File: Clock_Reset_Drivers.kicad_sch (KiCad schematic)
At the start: 9 parts, among them J4 2Pin_Header_2.54, U3 SPC5676RDK3MVU1R

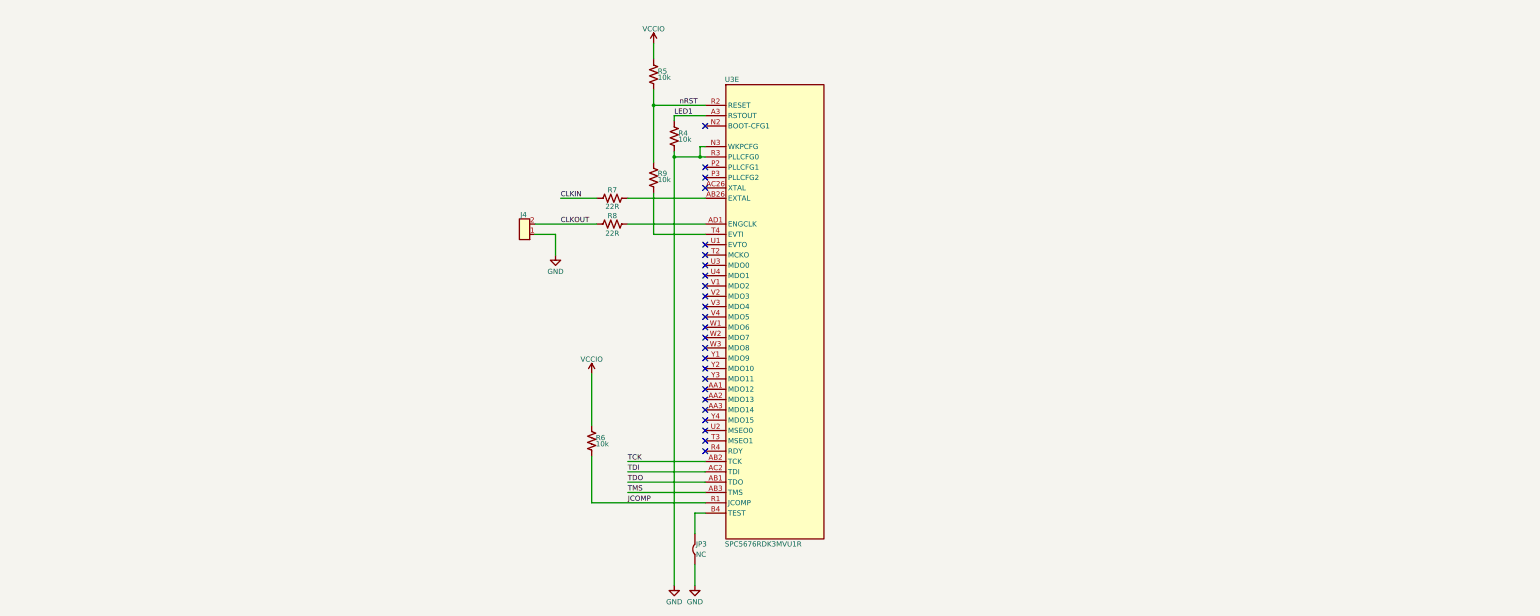
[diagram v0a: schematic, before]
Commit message: draft updated, schematic draft done, pcb issues with size of board and fitting all parts on
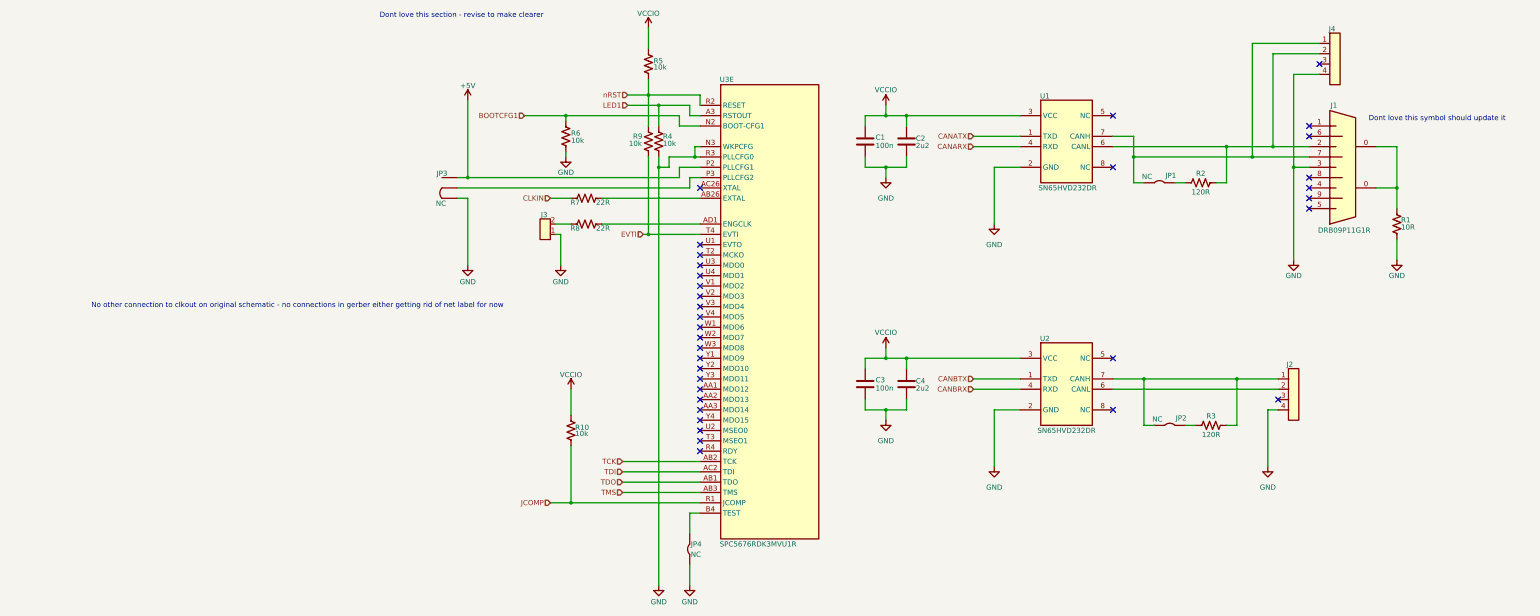
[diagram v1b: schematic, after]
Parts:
- added C1, C3: CAP_100n_16V_0402, Capacitor_SMD:C_0402_1005Metric, symbol nae_caps:CAP_100n_16V_0402
- added C2, C4: CAP_2u2_10V_0603, Capacitor_SMD:C_0603_1608Metric, symbol nae_caps:CAP_2u2_10V_0603
- added J1: DRB09P11G1R, Connector_Dsub:DSUB-9_Male_Horizontal_P2.77x2.84mm_EdgePinOffset9.90mm_Housed_MountingHolesOffset11.32mm, symbol tutorial_2_library:DB9_Connector_male
- added J2, J4: HDR_4_2.54, Connector_PinHeader_1.00mm:PinHeader_1x04_P1.00mm_Vertical, symbol tutorial_2_library:VERT_HDR_4_2.54mm_1
- added JP1, JP2: ~, Jumper:SolderJumper-2_P1.3mm_Bridged2Bar_Pad1.0x1.5mm, symbol tutorial_2_library:Solder_Jumper_2_NC
- added JP3: ~, Jumper:SolderJumper-3_P1.3mm_Bridged2Bar12_Pad1.0x1.5mm, symbol tutorial_2_library:Solder_Jumper_3_NC_1
- added R1: RES_10R_0603, Resistor_SMD:R_0603_1608Metric, symbol 0603_Yageo_Res:RES_10R_0603
- added R2, R3: RES_120R_0603, Resistor_SMD:R_0603_1608Metric, symbol 0603_Yageo_Res:RES_120R_0603
- added R6: RES_10k_0603, Resistor_SMD:R_0603_1608Metric, symbol 0603_Yageo_Res:RES_10k_0603
- added U1, U2: SN65HVD232DR, Package_SO:SOIC-8_3.9x4.9mm_P1.27mm, symbol tutorial_2_library:SN65HVD232DR
- renumbered J4 to J3, JP3 to JP4, R6 to R10
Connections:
- net GND: now also C1.1, C2.1, C3.1, C4.1, J1.3, J2.4, J4.4, JP3.1, R1.1, R6.1, U1.2 (GND), U2.2 (GND)
- net VCCIO: now also C1.2, C2.2, C3.2, C4.2, U1.3 (VCC), U2.3 (VCC)
- net BOOTCFG1: now reaches U3.N2 (BOOT-CFG1)
- net BOOTCFG1: now also R6.2
- net +5V: now reaches U3.P2 (PLLCFG1)
- net +5V: now also JP3.3
- net at U3.P3 (PLLCFG2): now also JP3.2
- net EVTI: now reaches R9.1, U3.T4 (EVTI)
- net CLKOUT: no longer names the net of J3.2, R8.1
- new net: JP1.1, R2.1
- new net: J1.7, J4.1, JP1.2, U1.7 (CANH)
- new net: J1.2, J4.2, R2.2, U1.6 (CANL)
- new net: J1.0, R1.2
- new net: J2.1, JP2.2, R3.2, U2.7 (CANH)
- new net: J2.2, U2.6 (CANL)
- new net: JP2.1, R3.1
- new net CANARX: U1.4 (RXD)
- new net CANATX: U1.1 (TXD)
- new net CANBRX: U2.4 (RXD)
- new net CANBTX: U2.1 (TXD)
- no-connect marks 25 -> 34
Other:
- note added: "Dont love this section - revise to make clearer"
- note added: "Dont love this symbol should update it"
- note added: "No other connection to clkout on original schematic - no connections in gerber either getting rid of net label for now"
- moved on the sheet: J3, JP4, R10, R4, R5, R7, R8, R9, U3E

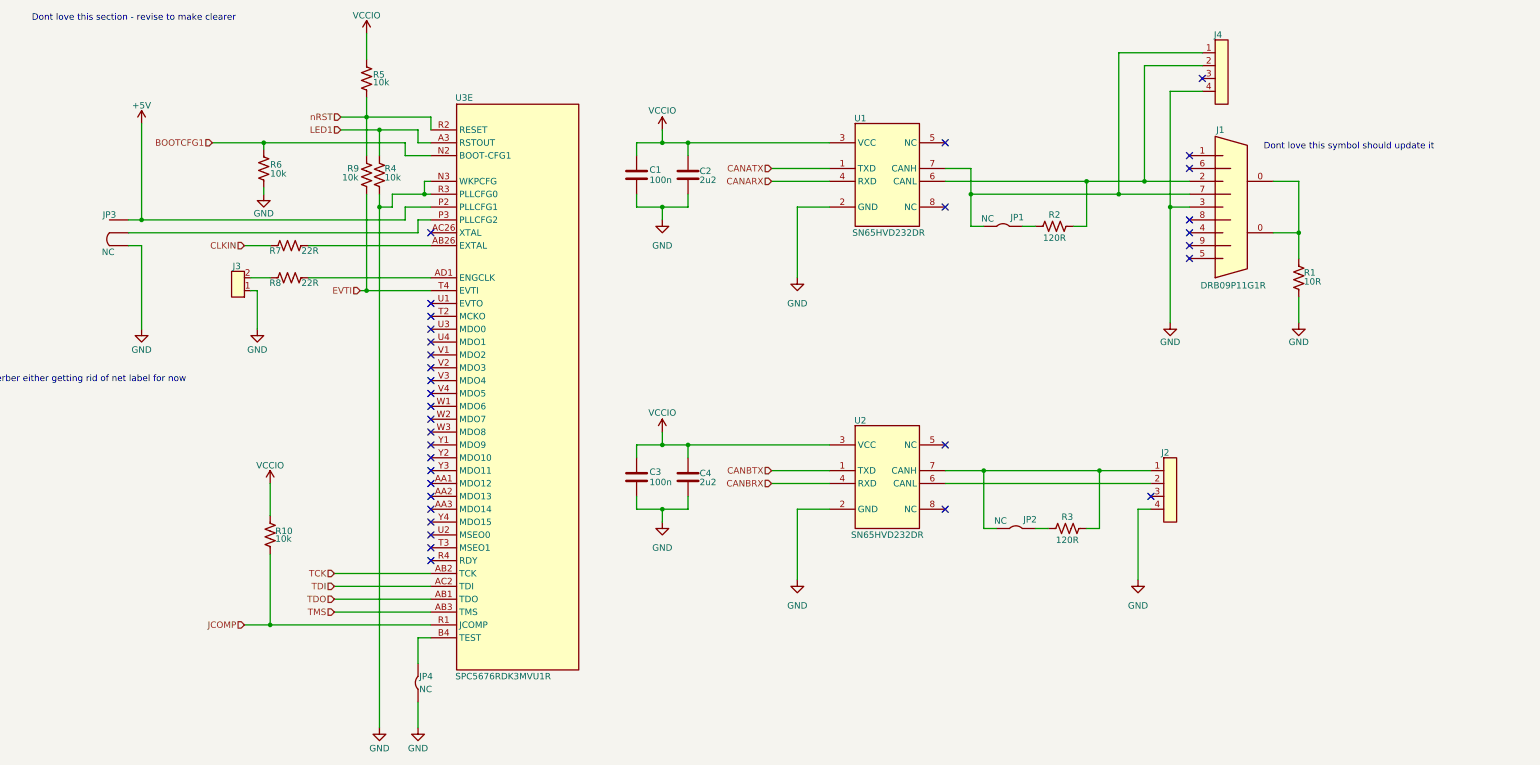
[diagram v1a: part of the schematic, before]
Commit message: updated schematic after library re-organization
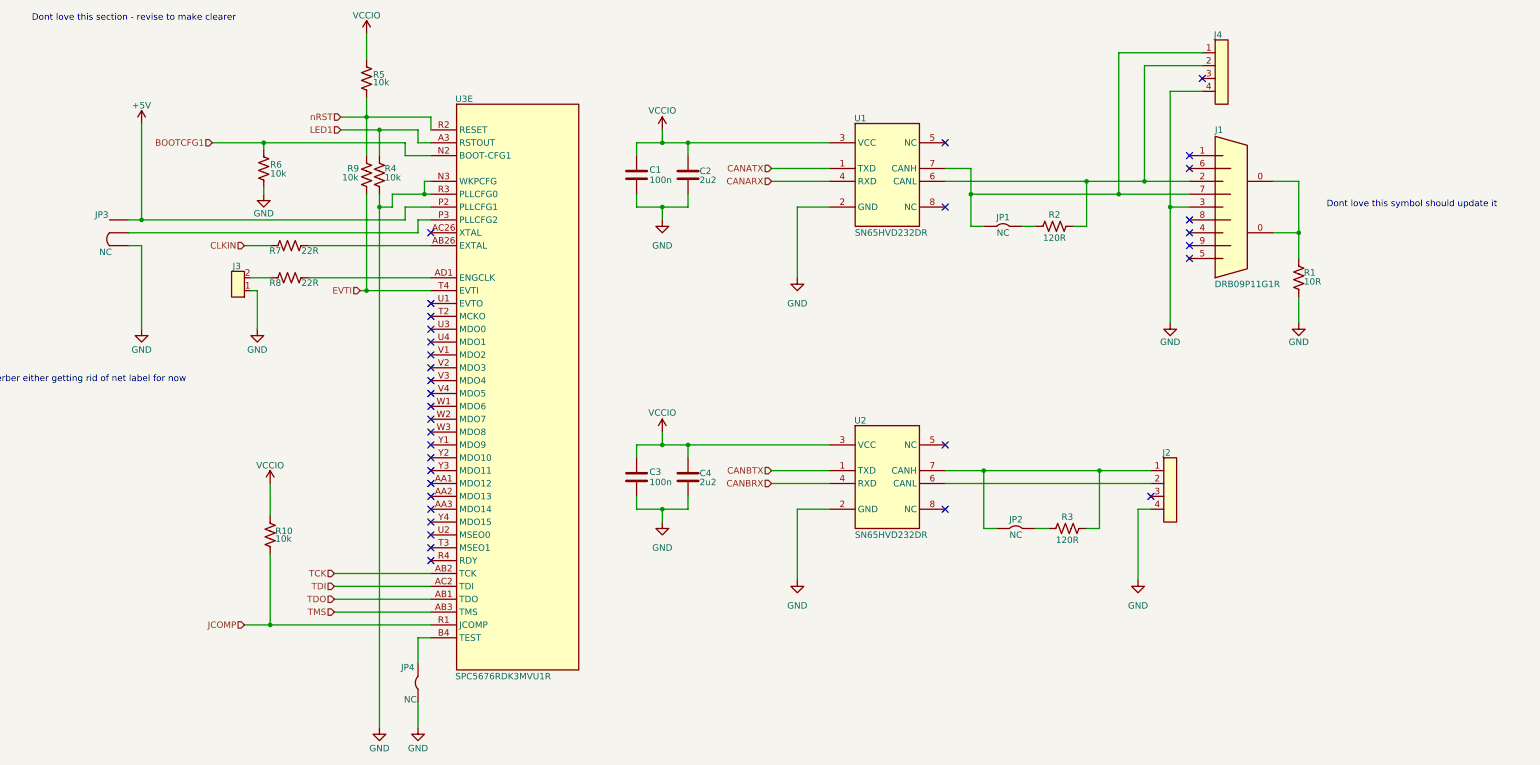
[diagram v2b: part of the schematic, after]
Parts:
- removed J1: DRB09P11G1R, Connector_Dsub:DSUB-9_Male_Horizontal_P2.77x2.84mm_EdgePinOffset9.90mm_Housed_MountingHolesOffset11.32mm, symbol tutorial_2_library:DB9_Connector_male
- removed J2, J4: HDR_4_2.54, Connector_PinHeader_1.00mm:PinHeader_1x04_P1.00mm_Vertical, symbol tutorial_2_library:VERT_HDR_4_2.54mm_1
- removed J3: 2Pin_Header_2.54, Connector_PinHeader_2.54mm:PinHeader_2x01_P2.54mm_Vertical, symbol tutorial_2_library:HEADER_2_2.54MM
- removed JP1, JP2, JP4: ~, Jumper:SolderJumper-2_P1.3mm_Bridged2Bar_Pad1.0x1.5mm, symbol tutorial_2_library:Solder_Jumper_2_NC
- removed JP3: ~, Jumper:SolderJumper-3_P1.3mm_Bridged2Bar12_Pad1.0x1.5mm, symbol tutorial_2_library:Solder_Jumper_3_NC_1
- removed U1, U2: SN65HVD232DR, Package_SO:SOIC-8_3.9x4.9mm_P1.27mm, symbol tutorial_2_library:SN65HVD232DR
- removed U3: SPC5676RDK3MVU1R, tutorial_2_library:BGA416C100P26X26_2700X2700X255N, symbol tutorial_2_library:SPC5676RDK3MVU1R
- added J1: DRB09P11G1R, Connector_Dsub:DSUB-9_Male_Horizontal_P2.77x2.84mm_EdgePinOffset9.90mm_Housed_MountingHolesOffset11.32mm, symbol NAE_Connectors:DB9_Connector_male
- added J2, J4: HDR_4_2.54, Connector_PinHeader_2.54mm:PinHeader_1x04_P2.54mm_Vertical, symbol NAE_Connectors:VERT_HDR_4_2.54mm
- added J3: 2Pin_Header_2.54, Connector_PinHeader_2.54mm:PinHeader_2x01_P2.54mm_Vertical, symbol NAE_Connectors:VERT_HDR_2_2.54mm
- added JP1, JP2, JP4: ~, Jumper:SolderJumper-2_P1.3mm_Bridged2Bar_Pad1.0x1.5mm, symbol NAE_Connectors:Solder_Jumper_2_NC
- added JP3: ~, Jumper:SolderJumper-3_P1.3mm_Bridged2Bar12_Pad1.0x1.5mm, symbol NAE_Connectors:Solder_Jumper_3_NC_1
- added U1, U2: SN65HVD232DR, Package_SO:SOIC-8_3.9x4.9mm_P1.27mm, symbol NAE_Integrated_Circuits:SN65HVD232DR
- added U3: SPC5676RDK3MVU1R, tutorial_2_library:BGA416C100P26X26_2700X2700X255N, symbol NAE_Integrated_Circuits:SPC5676RDK3MVU1R
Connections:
- net +5V: now also JP3.3, U3.P2 (PLLCFG1)
- net BOOTCFG1: now also U3.N2 (BOOT-CFG1)
- net CANARX: now also U1.4 (RXD)
- net CANATX: now also U1.1 (TXD)
- net CANBRX: now also U2.4 (RXD)
- net CANBTX: now also U2.1 (TXD)
- net EVTI: now also U3.T4 (EVTI)
- net GND: now also J1.3, J2.4, J3.1, J4.4, JP3.1, JP4.2, U1.2 (GND), U2.2 (GND), U3.N3 (WKPCFG), U3.R3 (PLLCFG0)
- net JCOMP: now also U3.R1 (JCOMP)
- net LED1: now also U3.A3 (RSTOUT)
- net TCK: now also U3.AB2 (TCK)
- net TDI: now also U3.AC2 (TDI)
- net TDO: now also U3.AB1 (TDO)
- net TMS: now also U3.AB3 (TMS)
- net VCCIO: now also U1.3 (VCC), U2.3 (VCC)
- net nRST: now also U3.R2 (RESET)
- net at R7.2: now also U3.AB26 (EXTAL)
- net at R8.2: now also U3.AD1 (ENGCLK)
- net at R2.1: now also JP1.1
- net at R8.1: now also J3.2
- net at R2.2: now also J1.2, J4.2, U1.6 (CANL)
- net at R1.2: now also J1.0
- net at R3.2: now also J2.1, JP2.2, U2.7 (CANH)
- net at R3.1: now also JP2.1
- new net: J2.2, U2.6 (CANL)
- new net: J1.7, J4.1, JP1.2, U1.7 (CANH)
- new net: JP3.2, U3.P3 (PLLCFG2)
- new net: JP4.1, U3.B4 (TEST)
